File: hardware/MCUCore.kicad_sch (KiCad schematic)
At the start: 11 parts, among them J1 UART_HDR, J2 EXP_HDR, SW1 RESET, SW2 BOOT, U1 ESP32-WROOM-32E

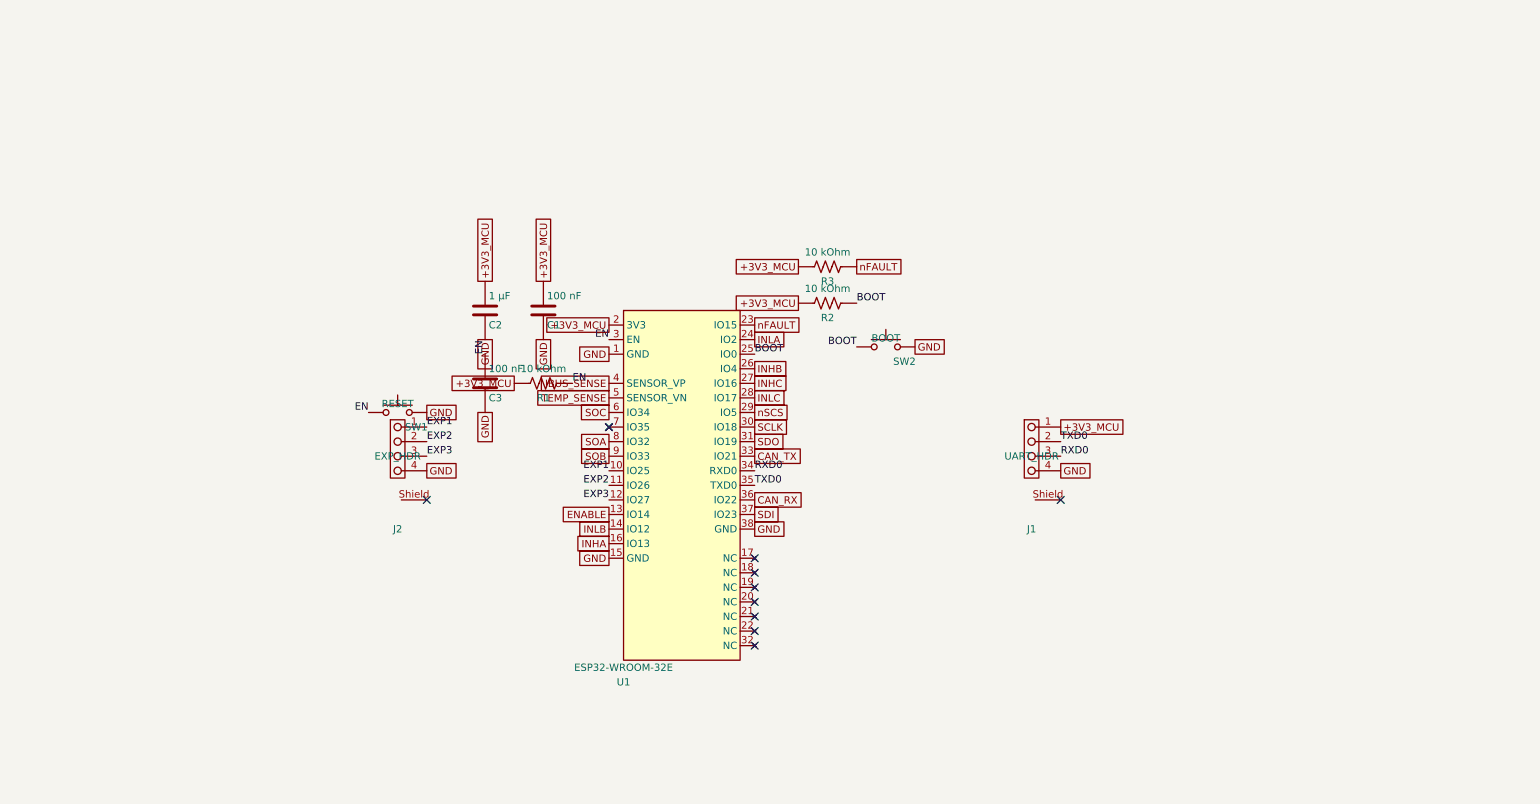
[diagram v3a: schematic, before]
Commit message: Schematic Rev B: full rebuild per METU PowerLab rules
Rev A was withdrawn: labels stuck on pins created real net shorts
(+5V_LOGIC with the 36 V bus, INHA and EFUSE_IMON with GND) and several
circuits contradicted their datasheets.

Rev B: real wires and power symbols on the 2.54 mm grid, hierarchical sheets
(half bridge reused 3x), library values, LAYOUT notes, root page with specs
and block diagram. Circuit fixes: DRV8323 VREF driven, unused buck tied to
GND, INA240A1, LM74700-Q1 reverse polarity, SMBJ36CA, eFuse per datasheet,
direct 3.3 V buck, 4.7 uH/8.1 A inductor, 2512 shunts with net-tie Kelvin,
24 V CAN ESD. kicad-cli ERC: 0 errors; netlist matches intent on all nets.
Old board and project-local library tables removed (board is rebuilt next).

Co-Authored-By: Claude Opus 5.5 <noreply@anthropic.com>
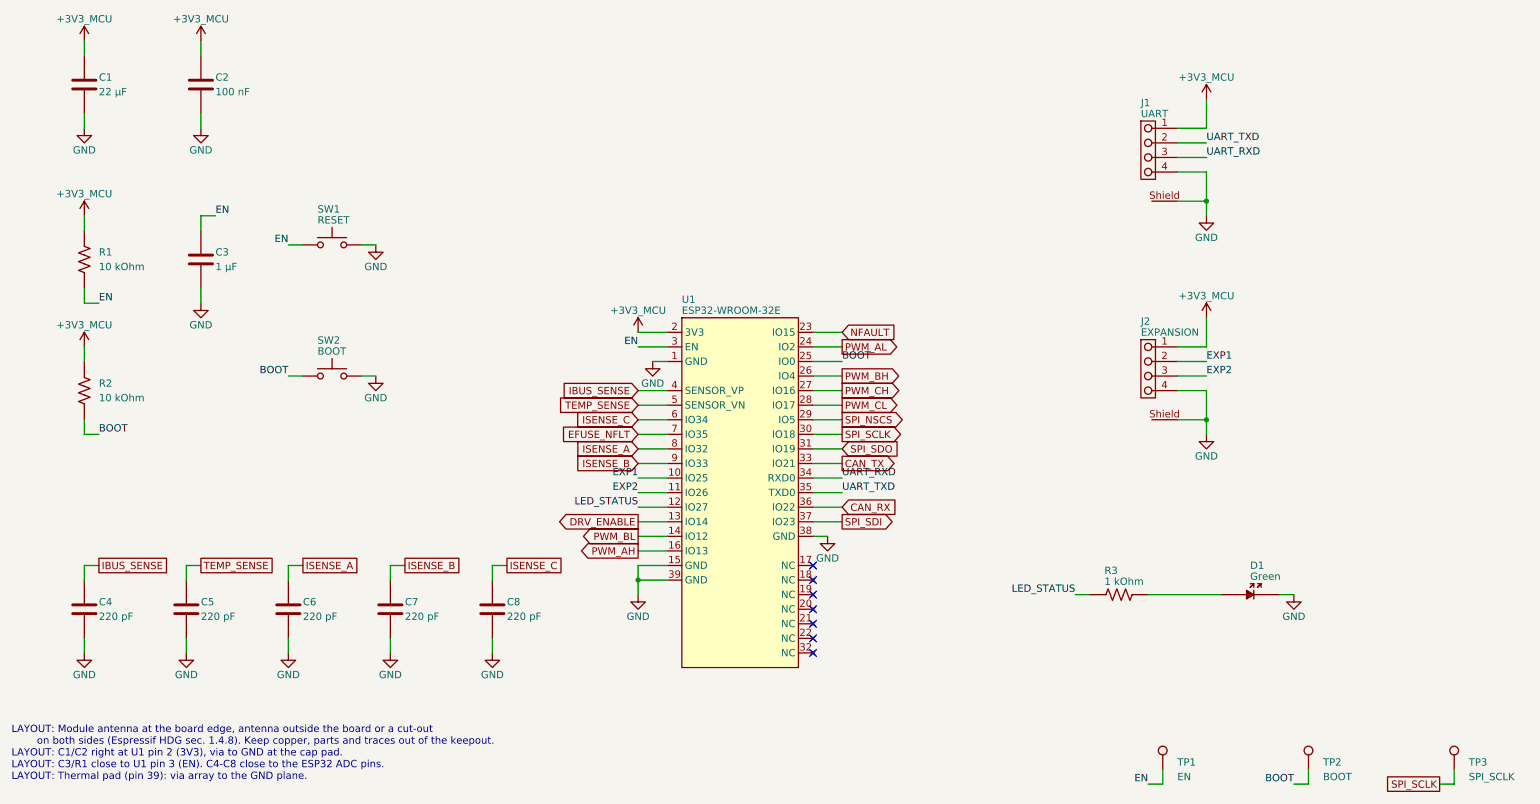
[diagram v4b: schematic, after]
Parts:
- removed C1, C3: 100 nF, METUPowerLab_Capacitors_Ceramics_SurfaceMounts:0603_Medium, symbol METUPowerLab_Capacitors_Ceramics_SurfaceMounts:100 nF
- removed C2: 1 µF, METUPowerLab_Capacitors_Ceramics_SurfaceMounts:0603_Medium, symbol METUPowerLab_Capacitors_Ceramics_SurfaceMounts:1 µF
- removed R3: 10 kOhm, METUPowerLab_Resistors_ChipResistors:0603_Medium, symbol METUPowerLab_Resistors_ChipResistors:10 kOhm
- added C1: 22 µF, METUPowerLab_Capacitors_Ceramics_SurfaceMounts:0603_Medium, symbol METUPowerLab_Capacitors_Ceramics_SurfaceMounts:22 µF
- added C2: 100 nF, METUPowerLab_Capacitors_Ceramics_SurfaceMounts:0603_Medium, symbol METUPowerLab_Capacitors_Ceramics_SurfaceMounts:100 nF
- added C3: 1 µF, METUPowerLab_Capacitors_Ceramics_SurfaceMounts:0603_Medium, symbol METUPowerLab_Capacitors_Ceramics_SurfaceMounts:1 µF 0603
- added C4, C5, C6, C7, C8: 220 pF, METUPowerLab_Capacitors_Ceramics_SurfaceMounts:0603_Medium, symbol METUPowerLab_Capacitors_Ceramics_SurfaceMounts:220 pF
- added D1: Green, METUPowerLab_LEDs_SurfaceMounts:0603_Medium, symbol METUPowerLab_LEDs_SurfaceMounts:Green
- added R3: 1 kOhm, METUPowerLab_Resistors_ChipResistors:0603_Medium, symbol METUPowerLab_Resistors_ChipResistors:1 kOhm
- added TP1: EN, METUPowerLab_TestPoints_SurfaceMounts:Pad_D1.5mm, symbol METUPowerLab_TestPoints_SurfaceMounts:TestPoint_Pad
- added TP2: BOOT, METUPowerLab_TestPoints_SurfaceMounts:Pad_D1.5mm, symbol METUPowerLab_TestPoints_SurfaceMounts:TestPoint_Pad
- added TP3: SPI_SCLK, METUPowerLab_TestPoints_SurfaceMounts:Pad_D1.5mm, symbol METUPowerLab_TestPoints_SurfaceMounts:TestPoint_Pad
- J1: value UART_HDR -> UART; Contact Type (none) -> Forked; Current Rating (none) -> 1.5A; Digi-Key Number (none) -> 900-2147210040CT-ND; Manufacturer (none) -> Molex; Manufacturer Number (none) -> 2147210040; Mounting Type (none) -> Surface Mount, Right Angle; Mouser Number (none) -> 538-214721-0040; Number of Positions (none) -> 4; Number of Rows (none) -> 1; Operating Temperature (none) -> -40°C up to 85°C; Voltage Rating (none) -> 30V
- J2: value EXP_HDR -> EXPANSION; Contact Type (none) -> Male Pin; Current Rating (none) -> 12A per Contact; Digi-Key Number (none) -> 2684-384471-ECT-ND; Farnell Number (none) -> 4060713; Manufacturer (none) -> TE Connectivity Erni; Manufacturer Number (none) -> 384471-E; Mounting Type (none) -> Surface Mount, Right Angle; Mouser Number (none) -> 305-384471; Number of Positions (none) -> 4; Number of Rows (none) -> 1; Operating Temperature (none) -> -55°C up to 150°C; Voltage Rating (none) -> -
- R1, R2: Digi-Key Number (none) -> 311-10.0KHRCT-ND; Farnell Number (none) -> 2421850; Manufacturer (none) -> YAGEO; Manufacturer Number (none) -> RC0603FR-0710KL; Mounting Type (none) -> Surface Mount; Mouser Number (none) -> 603-RC0603FR-0710KL; Operating Temperature (none) -> -55°C up to 155°C; Package (none) -> 0603 (1608 Metric); Power (none) -> 1/10 Watt; Tolerance (none) -> ±1%; Özdisan Number (none) -> RC0603FR-0710KL
- SW1, SW2: Contact Rating @ Voltage (none) -> 0.05A @ 32VDC; Digi-Key Number (none) -> EG5546CT-ND; Manufacturer (none) -> E-Switch; Manufacturer Number (none) -> TL6330AF200Q; Mechanical Life (none) -> 200,000 Cycles; Mounting Type (none) -> Surface Mount; Mouser Number (none) -> 612-TL6330AF200Q; Operating Temperature (none) -> -40°C up to 85°C; Package (none) -> 3.7*2.8mm
- U1: Digi-Key Number (none) -> 1965-ESP32-WROOM-32E-N4CT-ND; Manufacturer (none) -> Espressif Systems; Manufacturer Number (none) -> ESP32-WROOM-32E-N4; Mounting Type (none) -> Surface Mount; Mouser Number (none) -> 356-ESP32WRM32E132PH; Package (none) -> Module 18x25.5mm; Özdisan Number (none) -> ESP32-WROOM-32E-N4
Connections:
- net +3V3_MCU: now also J2.1, C1.1, C2.1
- net BOOT: now also TP2.1
- net EN: now also C3.1, TP1.1
- net EXP1: now also J2.2; no longer J2.1
- net EXP2: now also J2.3; no longer J2.2
- net GND: now also J1.Shield, J2.Shield, U1.39 (GND), C1.2, C2.2, C3.2, C4.2, C5.2, C6.2, C7.2, C8.2, D1.2
- net IBUS_SENSE: now also C4.1
- net TEMP_SENSE: now also C5.1
- net EFUSE_NFLT: now reaches U1.7 (IO35)
- net ENABLE renamed DRV_ENABLE
- net EXP3 renamed LED_STATUS
- net LED_STATUS: now also R3.1; no longer J2.3
- net INHA renamed PWM_AH
- net INHB renamed PWM_BH
- net INHC renamed PWM_CH
- net INLA renamed PWM_AL
- net INLB renamed PWM_BL
- net INLC renamed PWM_CL
- net RXD0 renamed UART_RXD
- net SCLK renamed SPI_SCLK
- net SPI_SCLK: now also TP3.1
- net SDI renamed SPI_SDI
- net SDO renamed SPI_SDO
- net SOA renamed ISENSE_A
- net ISENSE_A: now also C6.1
- net SOB renamed ISENSE_B
- net ISENSE_B: now also C7.1
- net SOC renamed ISENSE_C
- net ISENSE_C: now also C8.1
- net TXD0 renamed UART_TXD
- net nFAULT renamed NFAULT
- net nSCS renamed SPI_NSCS
- new net: D1.1, R3.2
- no-connect marks 11 -> 7
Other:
- note added: "LAYOUT: Module antenna at the board edge, antenna outside the board or a cut-out on both sides (Espressif HDG sec. 1.4.8). Keep copper, parts and traces out of the keepout. LAYOUT: C1/C2 right at U1 pin 2 (3V3), via to GND at the cap pad. LAYOUT: C3/R1 close to U1 pin 3 (EN). C4-C8 close to the ESP32 ADC pins. LAYOUT: Thermal pad (pin 39): via array to the GND plane."
- title: ${PROJECT_NAME} -> MCU Core
